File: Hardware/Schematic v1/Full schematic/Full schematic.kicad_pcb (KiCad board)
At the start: 2 copper layers, 159.3 x 59.9 mm, 329 parts, among them J1 Conn_01x02_Male, J10 Conn_01x01_Male, J2 Reset, J3 Encoder, J4 Failure LED, J5 Bluetooth, J6 Conn_01x02_Male, J7 Display, J8 Buttons, J9 Conn_01x02_Male, K1 EDR101A0500, K2 EDR101A0500, K3 EDR101A0500, K4 EDR101A0500, K5 EDR101A0500, K6 EDR101A0500, Q1 BC847, Q10 IRLML6402, Q11 BC847, Q12 IRFZ44, Q13 BC847, Q14 BSS138, Q15 BC847, Q16 IRF610, Q17 BC847, Q18 IRLML6402, Q19 BC847, Q2 BC847, Q20 BFS17, Q21 IRLML6402, Q22 AFT05MS003N, Q23 IRLML2502, Q24 IRLML2502, Q25 IRLML2502, Q26 IRLML2502, Q27 IRLML2502, Q28 IRLML2502, Q3 BC847, Q4 BC847, Q5 BC847, Q6 IRLML6402, Q7 IRF4905, Q8 IRLML6402, Q9 IRLML6402, U1 74LVC2T45DC, U10 ICS501, U11 STM32F103C8Tx, U12 CAT24C256, U2 74LVC2T45DC, U3 AD9835, U4 LM27313XMF, U5 LM2734X, U6 LM2734X, U7 LM2734X, U8 UC3843_SOIC8, U9 AD5245BRJZ10, X1 50MHz, Y1 8MHz, Y2 32768Hz

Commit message: Prepared to start PCB tracing
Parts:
- removed C107: 200pF, Capacitor_SMD:C_0805_2012Metric_Pad1.18x1.45mm_HandSolder
- removed C108, C109, C112: 0.1uF, Capacitor_SMD:C_0805_2012Metric_Pad1.18x1.45mm_HandSolder
- removed C110: 100uF x 16V, Capacitor_THT:CP_Radial_D6.3mm_P2.50mm
- removed C111: 22uF x 10V, Capacitor_THT:CP_Radial_D4.0mm_P2.00mm
- removed C113: 56pF, Capacitor_SMD:C_0805_2012Metric_Pad1.18x1.45mm_HandSolder
- removed C114, C115, C116, C117, C118, C119: 100pF, Capacitor_SMD:C_0805_2012Metric_Pad1.18x1.45mm_HandSolder
- removed C120, C121, C122, C123, C124, C125: 47pF, Capacitor_SMD:C_0805_2012Metric_Pad1.18x1.45mm_HandSolder
- removed C126, C127, C128, C129, C130, C131: 24pF, Capacitor_SMD:C_0805_2012Metric_Pad1.18x1.45mm_HandSolder
- removed C132, C133, C134, C135, C136, C137: 12pF, Capacitor_SMD:C_0805_2012Metric_Pad1.18x1.45mm_HandSolder
- removed D14: 1N4728A, Diode_THT:D_DO-41_SOD81_P10.16mm_Horizontal
- added Q29: IRLML2502, Package_TO_SOT_SMD:SOT-23, F.Cu at (104.5, 174.7)
- added Q30: IRLML2502, Package_TO_SOT_SMD:SOT-23, F.Cu at (172.8, 109.2)
- added R98: 100, Resistor_SMD:R_0805_2012Metric_Pad1.20x1.40mm_HandSolder, F.Cu at (138.6, 164.3)
- added R99: 100, Resistor_SMD:R_0805_2012Metric_Pad1.20x1.40mm_HandSolder, F.Cu at (119.0, 181.0)
- C1, C10, C11, C12, C18, C2, C3, C48, C7, C76, C8, C9, J1, J10, J2, J3, J4, J5, J6, J7, J8, J9, JP1, JP2, JP3, JP4, L13, L14, L15, L8, Q12, Q7, R45, R46, R88, R90, R92, RV1, RV2, X1, Y1, Y2: moved to F.Cu
- C100: value 0.1uF -> 56pF; moved to F.Cu
- C101: value 20pF -> 16pF 250V
- C102: value 200pF -> 8pF 250V
- C103: value 200pF -> 4pF 250V
- C104: value 200pF -> 2pF 250V
- C105: value 200pF -> 0.1uF
- C106: value 200pF -> 22uF x 10V; footprint Capacitor_SMD:C_0805_2012Metric_Pad1.18x1.45mm_HandSolder -> Capacitor_THT:CP_Radial_D4.0mm_P2.00mm
- C23, C85: value 4.7uF -> 0.1uF; moved to F.Cu
- C24, C65: value 0.1uF -> 4.7uF
- C28: value 10nF -> 1000uF x 10V; footprint Capacitor_SMD:C_0805_2012Metric_Pad1.18x1.45mm_HandSolder -> Capacitor_THT:CP_Radial_D10.0mm_P5.00mm
- C29: value 1000uF x 10V -> 47pF; footprint Capacitor_THT:CP_Radial_D10.0mm_P5.00mm -> Capacitor_SMD:C_0805_2012Metric_Pad1.18x1.45mm_HandSolder; moved to F.Cu
- C31: value 47pF -> 10nF
- C32: value 10nF -> 100pF
- C33: value 100pF -> 1nF
- C39, C55: value 1nF -> 4.7uF
- C41: value 1nF -> 47pF
- C44: value 47pF -> 220uFx6.3V; footprint Capacitor_SMD:C_0805_2012Metric_Pad1.18x1.45mm_HandSolder -> Capacitor_THT:CP_Radial_D6.3mm_P2.50mm
- C47: value 4.7uF -> 220uFx6.3V; footprint Capacitor_SMD:C_0805_2012Metric_Pad1.18x1.45mm_HandSolder -> Capacitor_THT:CP_Radial_D6.3mm_P2.50mm
- C49: value 220uFx6.3V -> 1nF; footprint Capacitor_THT:CP_Radial_D6.3mm_P2.50mm -> Capacitor_SMD:C_0805_2012Metric_Pad1.18x1.45mm_HandSolder; moved to F.Cu
- C50: value 220uFx6.3V -> 4.7uF; footprint Capacitor_THT:CP_Radial_D6.3mm_P2.50mm -> Capacitor_SMD:C_0805_2012Metric_Pad1.18x1.45mm_HandSolder; moved to F.Cu
- C51: value 1nF -> 1000uF x 25V; footprint Capacitor_SMD:C_0805_2012Metric_Pad1.18x1.45mm_HandSolder -> Capacitor_THT:CP_Radial_D10.0mm_P5.00mm
- C52, C60, C67: value 4.7uF -> 0.1uF
- C53: value 1000uF x 25V -> 1nF; footprint Capacitor_THT:CP_Radial_D10.0mm_P5.00mm -> Capacitor_SMD:C_0805_2012Metric_Pad1.18x1.45mm_HandSolder; moved to F.Cu
- C57: value 4.7uF -> 1000uF x 25V; footprint Capacitor_SMD:C_0805_2012Metric_Pad1.18x1.45mm_HandSolder -> Capacitor_THT:CP_Radial_D10.0mm_P5.00mm
- C58: value 1000uF x 25V -> 4.7uF; footprint Capacitor_THT:CP_Radial_D10.0mm_P5.00mm -> Capacitor_SMD:C_0805_2012Metric_Pad1.18x1.45mm_HandSolder; moved to F.Cu
- C61, C74: value 0.1uF -> 10nF
- C63, C93: value 10nF -> 0.1uF
- C68: value 0.1uF -> 1nF
- C70: value 0.1uF -> 75pF
- C71: value 1nF -> 10nF
- C72: value 75pF -> 0.1uF
- C73: value 10nF -> 100uFx6.3V; footprint Capacitor_SMD:C_0805_2012Metric_Pad1.18x1.45mm_HandSolder -> Capacitor_THT:CP_Radial_D6.3mm_P2.50mm
- C75: value 100uFx6.3V -> 1nF; footprint Capacitor_THT:CP_Radial_D6.3mm_P2.50mm -> Capacitor_SMD:C_0805_2012Metric_Pad1.18x1.45mm_HandSolder; moved to F.Cu
- C77: value 1nF -> 22pF
- C78: value 10nF -> 22pF; moved to F.Cu
- C79: value 22pF -> 10nF
- C80: value 22pF -> 8pF
- C81: value 10nF -> 8pF; moved to F.Cu
- C82: value 8pF -> 75pF
- C83: value 8pF -> 4.7uF
- C84: value 75pF -> 2pF 250V
- C86: value 0.1uF -> 62pF 250V; moved to F.Cu
- C87, C89: value 390pF -> 10nF
- C88, C92: value 390pF -> 0.1uF
- C90, C91: value 390pF -> 1nF
- C94: value 0.1uF -> 32pF 250V; moved to F.Cu
- C95: value 10nF -> 20pF
- C96, C97: value 1nF -> 0.1uF
- C98: value 0.1uF -> 100uF x 16V; footprint Capacitor_SMD:C_0805_2012Metric_Pad1.18x1.45mm_HandSolder -> Capacitor_THT:CP_Radial_D6.3mm_P2.50mm; moved to F.Cu
- D11: value 1N4148W -> 1N5819; footprint Diode_SMD:D_SOD-123 -> Diode_THT:D_DO-27_P5.08mm_Vertical_AnodeUp
- D12: value 1N5819 -> 1N4148W; footprint Diode_THT:D_DO-27_P5.08mm_Vertical_AnodeUp -> Diode_SMD:D_SOD-123; moved to F.Cu
- D13: value 1N4148W -> 1N4728A; footprint Diode_SMD:D_SOD-123 -> Diode_THT:D_DO-41_SOD81_P10.16mm_Horizontal
- K1, K2, K3, K4, K5, K6: value EDR101A0500 -> G6L-1F-DC5; footprint Relay_THT:Relay_SPST_StandexMeder_SIL_Form1A -> SamacSys:G6L-1F-DC5; moved to F.Cu
- L12: value 21uH -> 13uH; moved to F.Cu
- L5: value 10uH -> 22uH
- Q14: value BSS138 -> IRLML6402
- Q16: value IRF610 -> BSS138; footprint Package_TO_SOT_THT:TO-220-3_Vertical -> Package_TO_SOT_SMD:SOT-23; moved to F.Cu
- Q18: value IRLML6402 -> IRF610; footprint Package_TO_SOT_SMD:SOT-23 -> Package_TO_SOT_THT:TO-220-3_Vertical
- Q20: value BFS17 -> IRLML6402
- Q21: value IRLML6402 -> BC847
- Q22: value AFT05MS003N -> IRLML6402; footprint Package_TO_SOT_SMD:SOT-89-3_Handsoldering -> Package_TO_SOT_SMD:SOT-23
- Q23: value IRLML2502 -> BFS17
- Q24: value IRLML2502 -> AFT05MS003N; footprint Package_TO_SOT_SMD:SOT-23 -> Package_TO_SOT_SMD:SOT-89-3_Handsoldering
- R23: value 10k -> 47k
- R24, R70: value 4.7k -> 10k
- R25, R89, R93, R94: value 100 -> 4.7k
- R28: value 1.3k -> 100
- R29: value 150k -> 1.3k
- R30: value 12k -> 300
- R31: value 300 -> 150k
- R32: value 13k -> 12k
- R34: value 120k -> 13k
- R35: value 13k -> 120k
- R36: value 51k -> 13k
- R37: value 10k -> 51k
- R38: value 39k -> 10k
- R39, R77: value 10k -> 39k
- R40, R50: value 30k -> 10k
- R41: value 10k -> 10
- R42: value 10 -> 10k
- R43: value 10k -> 1k
- R44: value 1k -> 1; footprint Resistor_SMD:R_0805_2012Metric_Pad1.20x1.40mm_HandSolder -> Resistor_THT:R_Axial_DIN0207_L6.3mm_D2.5mm_P2.54mm_Vertical
- R47: value 1 -> 4.7k; footprint Resistor_THT:R_Axial_DIN0207_L6.3mm_D2.5mm_P2.54mm_Vertical -> Resistor_SMD:R_0805_2012Metric_Pad1.20x1.40mm_HandSolder; moved to F.Cu
- R48: value 4.7k -> 1; footprint Resistor_SMD:R_0805_2012Metric_Pad1.20x1.40mm_HandSolder -> Resistor_THT:R_Axial_DIN0207_L6.3mm_D2.5mm_P2.54mm_Vertical
- R49: value 1 -> 10k; footprint Resistor_THT:R_Axial_DIN0207_L6.3mm_D2.5mm_P2.54mm_Vertical -> Resistor_SMD:R_0805_2012Metric_Pad1.20x1.40mm_HandSolder; moved to F.Cu
- R51: value 6.8k -> 10
- R52: value 100 -> 30k
- R53: value 1k -> 6.8k
- R55: value 36k -> 1k
- R56: value 4.7k -> 100
- R57: value 56k -> 36k
- R58: value 30k -> 4.7k
- R59: value 6.8k -> 56k
- R60: value 1k -> 30k
- R61: value 100 -> 6.8k
- R62: value 3.9k -> 1k
- R63: value 2k -> 100
- R64: value 4.7k -> 3.9k
- R65: value 4.7k -> 2k
- R66: value 33k -> 4.7k
- R68: value 10k -> 33k
- R69: value 10k -> 4.7k
- R71: value 220k -> 4.7k
- R72: value 11k -> 10k
- R73: value 4.7k -> 220k
- R74: value 10 -> 11k
- R75: value 39k -> 4.7k
- R76: value 33 -> 10
- R78: value 4.7k -> 33
- R82: value 6.2k -> 10k
- R83: value 1k -> 4.7k
- R84: value 4.7k -> 6.2k
- R85: value 10 -> 1k
- R87: value 4.7k -> 10
- R91: value 4.7k -> 100; moved to F.Cu
- U7: value LM2734X -> MAX1837EUT33-T
- moved R34 153.7 mm to (191.8, 120.3), turned to 0 degrees
- moved R32 150.7 mm to (187.0, 120.4), turned to 0 degrees
- moved R30 149.4 mm to (191.3, 111.5), turned to 0 degrees
- moved R29 146.4 mm to (186.5, 114.5), turned to 0 degrees
- moved C30 141.0 mm to (176.9, 113.0), turned to 0 degrees
- moved C19 134.1 mm to (172.1, 113.0), turned to 0 degrees
- moved R37 133.7 mm to (182.3, 126.3), turned to 0 degrees
- moved C25 132.2 mm to (172.8, 125.0), turned to 0 degrees
- moved R39 130.9 mm to (191.3, 114.4), turned to 0 degrees
- moved L1 125.9 mm to (151.4, 109.5)
- moved C33 122.4 mm to (162.7, 120.8), turned to 0 degrees
- moved U5 120.7 mm to (162.3, 112.6), turned to 0 degrees
- moved L14 120.0 mm to (81.3, 128.3), turned to 0 degrees
- moved D5 119.1 mm to (162.6, 108.7), turned to 0 degrees
- moved Q3 118.4 mm to (167.3, 113.7), turned to 0 degrees
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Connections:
- C100 pad 1: REG_3.3V -> Net-(C100-Pad1)
- C101 pad 1: Net-(C101-Pad1) -> ANT_3.5
- C101 pad 2: GND -> Net-(C101-Pad2)
- C103 pad 1: Net-(C102-Pad2) -> ANT_3.5
- C104 pad 1: Net-(C103-Pad2) -> ANT_3.5
- C105 pad 1: Net-(C104-Pad2) -> PWR_3.5_5
- C105 pad 2: Net-(C105-Pad2) -> GND
- C106 pad 1: Net-(C105-Pad2) -> PWR_3.5_5
- C106 pad 2: Net-(C106-Pad2) -> GND
- C2 pad 1: REG_3.3V -> SW_3.3V
- C23 pad 1: PWR_3.5_12 -> Net-(C23-Pad1)
- C23 pad 2: GND -> Net-(C23-Pad2)
- C24 pad 1: Net-(C24-Pad1) -> PWR_3.5_12
- C24 pad 2: Net-(C24-Pad2) -> GND
- C28 pad 1: Net-(C28-Pad1) -> POWERS_3.5
- C28 pad 2: Net-(C28-Pad2) -> GND
- C29 pad 1: POWERS_3.5 -> Net-(C29-Pad1)
- C3 pad 1: REG_3.3V -> SW_3.3V
- C31 pad 2: GND -> Net-(C31-Pad2)
- C32 pad 1: Net-(C32-Pad1) -> Net-(C31-Pad1)
- C32 pad 2: Net-(C32-Pad2) -> GND
- C33 pad 1: Net-(C32-Pad1) -> REG_3.3V
- C39 pad 2: Net-(C39-Pad2) -> GND
- C41 pad 1: REG_5V -> Net-(C41-Pad1)
- C42 pad 1: DISPLAY_4V -> REG_5V
- C43 pad 1: REG_3.3V -> DISPLAY_4V
- C44 pad 1: Net-(C44-Pad1) -> REG_3.3V
- C47 pad 1: REG_3.3V -> REG_5V
- C48 pad 1: REG_5V -> DISPLAY_4V
- C49 pad 1: DISPLAY_4V -> Net-(C49-Pad1)
- C50 pad 1: REG_3.3V -> Net-(C49-Pad1)
- C51 pad 1: Net-(C51-Pad1) -> Net-(C49-Pad1)
- C52 pad 1: Net-(C51-Pad1) -> Net-(C52-Pad1)
- C52 pad 2: GND -> Net-(C52-Pad2)
- C53 pad 1: Net-(C51-Pad1) -> PWR_3.5_OUT
- C54 pad 2: Net-(C54-Pad2) -> Net-(C52-Pad1)
- C56 pad 1: Net-(C56-Pad1) -> PWR_3.5_12
- C56 pad 2: Net-(C54-Pad1) -> GND
- C58 pad 1: PWR_3.5_OUT -> PWR_3.5_12
- C59 pad 1: PWR_3.5_12 -> Net-(C59-Pad1)
- C59 pad 2: GND -> Net-(C59-Pad2)
- C60 pad 1: PWR_3.5_12 -> Net-(C60-Pad1)
- C61 pad 2: Net-(C61-Pad2) -> GND
- C62 pad 1: Net-(C62-Pad1) -> SW_3.3V
- C63 pad 2: GND -> Net-(C63-Pad2)
- C64 pad 1: REG_3.3V -> Net-(C64-Pad1)
- C65 pad 1: Net-(C65-Pad1) -> PWR_3.5_OUT
- C65 pad 2: Net-(C65-Pad2) -> GND
- C66 pad 1: Net-(C66-Pad1) -> PWR_3.5_OUT
- C67 pad 1: PWR_3.5_OUT -> Net-(C67-Pad1)
- C67 pad 2: GND -> Net-(C67-Pad2)
- C68 pad 1: PWR_3.5_OUT -> PWR_144_5
- C69 pad 1: Net-(C69-Pad1) -> RESET
- C69 pad 2: Net-(C69-Pad2) -> GND
- C70 pad 1: RESET -> Net-(C67-Pad1)
- C71 pad 1: PWR_144_5 -> Net-(C71-Pad1)
- C72 pad 1: Net-(C69-Pad1) -> PWR_144_5
- C73 pad 1: Net-(C73-Pad1) -> PWR_144_5
- C74 pad 1: PWR_144_5 -> ENCODER_BTN
- C75 pad 1: PWR_144_5 -> Net-(C75-Pad1)
- C75 pad 2: GND -> Net-(C75-Pad2)
- C76 pad 1: ENCODER_BTN -> ENCODER_R
- C77 pad 2: Net-(C77-Pad2) -> GND
- C78 pad 1: ENCODER_R -> Net-(C78-Pad1)
- C79 pad 1: Net-(C79-Pad1) -> ENCODER_L
- C81 pad 1: ENCODER_L -> Net-(C81-Pad1)
- C82 pad 2: GND -> Net-(C82-Pad2)
- C83 pad 1: Net-(C83-Pad1) -> REG_3.3V
- C84 pad 1: Net-(C84-Pad1) -> ANT_3.5
- C86 pad 1: REG_3.3V -> ANT_3.5
- C86 pad 2: GND -> Net-(C84-Pad2)
- C87 pad 1: ANT_3.5 -> BTN_RIGHT
- C87 pad 2: Net-(C87-Pad2) -> GND
- C88 pad 1: Net-(C87-Pad2) -> REG_3.3V
- C88 pad 2: Net-(C88-Pad2) -> GND
- C89 pad 1: Net-(C88-Pad2) -> BTN_LEFT
- C89 pad 2: Net-(C89-Pad2) -> GND
- C90 pad 1: Net-(C89-Pad2) -> PWR_144_OUT
- C90 pad 2: Net-(C90-Pad2) -> GND
- C91 pad 1: Net-(C90-Pad2) -> Net-(C91-Pad1)
- C92 pad 1: Net-(C91-Pad2) -> REG_3.3V
- C92 pad 2: Net-(C92-Pad2) -> GND
- C93 pad 1: BTN_RIGHT -> PWR_144_OUT
- C94 pad 1: REG_3.3V -> ANT_3.5
- C94 pad 2: GND -> Net-(C94-Pad2)
- C95 pad 1: BTN_LEFT -> Net-(C91-Pad1)
- C96 pad 1: PWR_144_OUT -> REG_3.3V
- C97 pad 1: Net-(C101-Pad1) -> GND
- C97 pad 2: Net-(C97-Pad2) -> SW_3.3V
- C98 pad 1: REG_3.3V -> PWR_144_OUT
- C99 pad 1: PWR_144_OUT -> REG_3.3V
- D10 pad 1: Net-(C28-Pad2) -> Net-(D10-Pad1)
- D10 pad 2: REG_3.3V -> Net-(D10-Pad2)
- D11 pad 1: Net-(D11-Pad1) -> Net-(C49-Pad1)
- D12 pad 1: Net-(C51-Pad1) -> Net-(C71-Pad1)
- D13 pad 1: Net-(C73-Pad1) -> ADC_UANT
- D13 pad 2: Net-(D13-Pad2) -> GND
- D7 pad 1: Net-(C28-Pad1) -> Net-(D7-Pad1)
- DA1 pad 3: Net-(C56-Pad1) -> Net-(C54-Pad1)
- J9 pad 2: Net-(C113-Pad1) -> Net-(C100-Pad1)
- K1 pad 1: Net-(C92-Pad2) -> Net-(C84-Pad2)
- K1 pad 3: PWR_3.5_5 -> Net-(K1-Pad3)
- K2 pad 1: Net-(C107-Pad2) -> Net-(C94-Pad2)
- K2 pad 3: PWR_3.5_5 -> Net-(K2-Pad3)
- K3 pad 1: Net-(C119-Pad2) -> Net-(C101-Pad2)
- K3 pad 3: PWR_3.5_5 -> Net-(K3-Pad3)
- K4 pad 1: Net-(C125-Pad2) -> Net-(C102-Pad2)
- K4 pad 3: PWR_3.5_5 -> Net-(K4-Pad3)
- K5 pad 1: Net-(C131-Pad2) -> Net-(C103-Pad2)
- K5 pad 3: PWR_3.5_5 -> Net-(K5-Pad3)
- K6 pad 1: Net-(C137-Pad2) -> Net-(C104-Pad2)
- K6 pad 3: PWR_3.5_5 -> Net-(K6-Pad3)
- L10 pad 1: Net-(C51-Pad1) -> Net-(C49-Pad1)
- L11 pad 2: Net-(C69-Pad2) -> Net-(C67-Pad2)
- L12 pad 1: Net-(C69-Pad1) -> Net-(C67-Pad1)
- L13 pad 2: Net-(C84-Pad2) -> Net-(C82-Pad2)
- L14 pad 2: Net-(C97-Pad2) -> Net-(C91-Pad2)
- L15 pad 1: Net-(C101-Pad1) -> Net-(C91-Pad1)
- L15 pad 2: Net-(C113-Pad1) -> Net-(C100-Pad1)
- L2 pad 1: Net-(C24-Pad1) -> Net-(C23-Pad1)
- L2 pad 2: Net-(C31-Pad1) -> Net-(C29-Pad1)
- L5 pad 1: Net-(C28-Pad1) -> Net-(D7-Pad1)
- L6 pad 1: Net-(C31-Pad1) -> Net-(C29-Pad1)
- L7 pad 2: Net-(C44-Pad1) -> Net-(C41-Pad1)
- L8 pad 2: Net-(D12-Pad2) -> Net-(D11-Pad2)
- L9 pad 1: Net-(C44-Pad1) -> Net-(C41-Pad1)
- L9 pad 2: Net-(C54-Pad1) -> Net-(C52-Pad1)
- Q12 pad 1: Net-(D11-Pad2) -> Net-(D10-Pad2)
- Q12 pad 2: Net-(D12-Pad2) -> Net-(D11-Pad2)
- Q13 pad 1: Net-(C54-Pad2) -> Net-(Q13-Pad1)
- Q13 pad 2: Net-(C62-Pad1) -> GND
- Q13 pad 3: Net-(C61-Pad2) -> Net-(Q13-Pad3)
- Q14 pad 2: GND -> REG_3.3V
- Q14 pad 3: Net-(C63-Pad1) -> SW_3.3V
- Q15 pad 1: Net-(C61-Pad1) -> Net-(C52-Pad2)
- Q15 pad 2: Net-(C66-Pad1) -> Net-(C60-Pad1)
- Q15 pad 3: Net-(C65-Pad2) -> Net-(C59-Pad2)
- Q16 pad 1: Net-(DA1-Pad6) -> Net-(Q16-Pad1)
- Q16 pad 2: Net-(C69-Pad2) -> GND
- Q16 pad 3: GND -> Net-(C61-Pad1)
- Q17 pad 1: Net-(Q17-Pad1) -> Net-(C59-Pad1)
- Q17 pad 2: GND -> Net-(C64-Pad1)
- Q17 pad 3: Net-(Q17-Pad3) -> Net-(C63-Pad2)
- Q18 pad 1: Net-(Q18-Pad1) -> Net-(DA1-Pad6)
- Q18 pad 2: REG_5V -> Net-(C67-Pad2)
- Q18 pad 3: BT_5V -> GND
- Q20 pad 1: Net-(C77-Pad1) -> Net-(Q20-Pad1)
- Q20 pad 2: GND -> REG_5V
- Q20 pad 3: Net-(C84-Pad2) -> BT_5V
- Q21 pad 2: PWR_144_5 -> GND
- Q21 pad 3: MANIP_144 -> Net-(Q21-Pad3)
- Q22 pad 1: Net-(C84-Pad1) -> Net-(Q22-Pad1)
- Q22 pad 2: GND -> PWR_144_5
- Q22 pad 3: Net-(C97-Pad2) -> MANIP_144
- Q23 pad 1: Net-(Q23-Pad1) -> Net-(C75-Pad1)
- Q23 pad 3: Net-(K1-Pad5) -> Net-(C82-Pad2)
- Q24 pad 1: Net-(Q24-Pad1) -> Net-(C82-Pad1)
- Q24 pad 3: Net-(K2-Pad5) -> Net-(C91-Pad2)
- Q25 pad 3: Net-(K3-Pad5) -> Net-(K1-Pad3)
- Q26 pad 3: Net-(K4-Pad5) -> Net-(K2-Pad3)
- Q27 pad 3: Net-(K5-Pad5) -> Net-(K3-Pad3)
- Q28 pad 3: Net-(K6-Pad5) -> Net-(K4-Pad3)
- R23 pad 1: Net-(Q6-Pad3) -> ACTIVATE_3.3V
- R23 pad 2: ADC_UBATT -> GND
- R24 pad 1: ADC_UBATT -> Net-(Q6-Pad3)
- R24 pad 2: GND -> ADC_UBATT
- R25 pad 1: Net-(R25-Pad1) -> ADC_UBATT
- R25 pad 2: Net-(R25-Pad2) -> GND
- R28 pad 1: Net-(Q11-Pad2) -> Net-(R28-Pad1)
- R28 pad 2: GND -> Net-(R28-Pad2)
- R29 pad 1: Net-(C19-Pad1) -> Net-(Q11-Pad2)
- R29 pad 2: Net-(C19-Pad2) -> GND
- R30 pad 1: Net-(C13-Pad1) -> Net-(C23-Pad2)
- R30 pad 2: Net-(C20-Pad1) -> GND
- R31 pad 1: Net-(C24-Pad2) -> Net-(C19-Pad1)
- R31 pad 2: GND -> Net-(C19-Pad2)
- R32 pad 1: Net-(C25-Pad2) -> Net-(C13-Pad1)
- R32 pad 2: GND -> Net-(C20-Pad1)
- R34 pad 1: PWR_3.5_12 -> Net-(C25-Pad2)
- R34 pad 2: Net-(C25-Pad2) -> GND
- R35 pad 1: Net-(C32-Pad2) -> PWR_3.5_12
- R35 pad 2: Net-(Q11-Pad2) -> Net-(C25-Pad2)
- R36 pad 1: REG_5V -> Net-(C31-Pad2)
- R36 pad 2: Net-(C37-Pad2) -> Net-(Q11-Pad2)
- R37 pad 1: Net-(C37-Pad2) -> REG_5V
- R37 pad 2: GND -> Net-(C37-Pad2)
- R38 pad 1: DISPLAY_4V -> Net-(C37-Pad2)
- R38 pad 2: Net-(C38-Pad2) -> GND
- R39 pad 1: Net-(C38-Pad2) -> DISPLAY_4V
- R39 pad 2: GND -> Net-(C38-Pad2)
- R40 pad 1: REG_3.3V -> Net-(C38-Pad2)
- R40 pad 2: Net-(C39-Pad2) -> GND
- R41 pad 1: Net-(C39-Pad2) -> Net-(D10-Pad2)
- R41 pad 2: GND -> Net-(D10-Pad1)
- R42 pad 1: Net-(D11-Pad2) -> Net-(D10-Pad2)
- R42 pad 2: Net-(D11-Pad1) -> GND
- R43 pad 1: Net-(D11-Pad2) -> Net-(Q12-Pad3)
- R43 pad 2: GND -> Net-(C31-Pad1)
- R44 pad 2: Net-(C32-Pad1) -> GND
- R47 pad 1: Net-(Q12-Pad3) -> Net-(C52-Pad1)
- R48 pad 1: Net-(C54-Pad1) -> Net-(Q12-Pad3)
- R49 pad 1: Net-(Q12-Pad3) -> Net-(Q13-Pad1)
- R49 pad 2: GND -> ACTIVATE_3.3V
- R50 pad 1: PWR_144_5 -> REG_3.3V
- R50 pad 2: Net-(C54-Pad2) -> Net-(Q14-Pad1)
- R51 pad 1: Net-(C54-Pad2) -> Net-(Q14-Pad1)
- R51 pad 2: GND -> Net-(Q13-Pad3)
- R52 pad 1: Net-(Q14-Pad1) -> PWR_144_5
- R52 pad 2: Manipulation -> Net-(C52-Pad2)
- R53 pad 1: PWR_144_5 -> Net-(C52-Pad2)
- R53 pad 2: Net-(C61-Pad2) -> GND
- R54 pad 1: Net-(C62-Pad1) -> Net-(Q16-Pad1)
- R54 pad 2: GND -> Manipulation
- R55 pad 1: PWR_3.5_OUT -> PWR_144_5
- R55 pad 2: Net-(C19-Pad2) -> Net-(C59-Pad2)
- R56 pad 1: Net-(C19-Pad2) -> Net-(C60-Pad1)
- R56 pad 2: Net-(R56-Pad2) -> GND
- R57 pad 1: PWR_3.5_12 -> PWR_3.5_OUT
- R57 pad 2: Net-(C63-Pad1) -> Net-(C19-Pad2)
- R58 pad 1: PWR_144_5 -> Net-(C19-Pad2)
- R58 pad 2: Net-(C61-Pad1) -> Net-(R58-Pad2)
- R59 pad 1: Net-(C61-Pad1) -> PWR_3.5_12
- R59 pad 2: GND -> Net-(C61-Pad1)
- R60 pad 2: Net-(C65-Pad2) -> Net-(C59-Pad1)
- R61 pad 1: Net-(C66-Pad1) -> Net-(C59-Pad1)
- R62 pad 1: Net-(DA1-Pad6) -> PWR_144_5
- R62 pad 2: Net-(DA1-Pad2) -> Net-(C63-Pad2)
- R63 pad 1: Net-(DA1-Pad2) -> Net-(C64-Pad1)
- R64 pad 1: PWR_144_5 -> Net-(DA1-Pad6)
- R64 pad 2: Net-(C65-Pad1) -> Net-(DA1-Pad2)
- R65 pad 1: Net-(C65-Pad1) -> Net-(DA1-Pad2)
- R66 pad 1: PWR_3.5_OUT -> PWR_144_5
- R66 pad 2: ADC_U3.5_OUT -> Net-(C63-Pad1)
- R67 pad 1: ADC_U3.5_OUT -> Net-(C63-Pad1)
- R68 pad 1: Net-(Q17-Pad1) -> PWR_3.5_OUT
- R68 pad 2: ENABLE_BT -> ADC_U3.5_OUT
- R69 pad 1: REG_5V -> ADC_U3.5_OUT
- R69 pad 2: Net-(Q18-Pad1) -> GND
- R70 pad 1: PWR_144_5 -> Net-(Q19-Pad1)
- R70 pad 2: Net-(R70-Pad2) -> ENABLE_BT
- R71 pad 1: ANT_3.5 -> PWR_144_5
- R71 pad 2: Net-(D13-Pad2) -> Net-(R71-Pad2)
- R72 pad 1: Net-(D13-Pad2) -> REG_5V
- R72 pad 2: GND -> Net-(Q20-Pad1)
- R73 pad 1: REG_3.3V -> ANT_3.5
- R73 pad 2: RESET -> Net-(D12-Pad2)
- R74 pad 1: Net-(Q18-Pad1) -> Net-(D12-Pad2)
- R74 pad 2: Net-(Q17-Pad3) -> GND
- R75 pad 1: ADC_UANT -> REG_3.3V
- R75 pad 2: Net-(C73-Pad1) -> RESET
- R76 pad 1: Net-(C77-Pad2) -> Net-(Q20-Pad1)
- R76 pad 2: GND -> Net-(Q19-Pad3)
- R77 pad 2: GND -> Net-(C71-Pad1)
- R78 pad 1: REG_3.3V -> Net-(C75-Pad2)
- R78 pad 2: ENCODER_BTN -> GND
- R79 pad 1: Net-(Q19-Pad1) -> ADC_UANT
- R79 pad 2: Manipulation -> GND
- R80 pad 1: REG_3.3V -> SW_3.3V
- R80 pad 2: ENCODER_R -> ENCODER_BTN
- R81 pad 1: PWR_144_5 -> Net-(Q21-Pad1)
- R81 pad 2: Net-(Q21-Pad1) -> Manipulation
- R82 pad 2: Net-(C77-Pad1) -> Net-(Q22-Pad1)
- R83 pad 1: Net-(C77-Pad1) -> SW_3.3V
- R83 pad 2: GND -> ENCODER_R
- R84 pad 1: REG_3.3V -> PWR_144_5
- R84 pad 2: ENCODER_L -> Net-(C75-Pad1)
- R85 pad 1: Net-(Q21-Pad1) -> Net-(C75-Pad1)
- R85 pad 2: Net-(Q19-Pad3) -> GND
- R86 pad 1: REG_3.3V -> SW_3.3V
- R86 pad 2: DISPLAY_SCL -> ENCODER_L
- R87 pad 1: REG_3.3V -> Net-(Q22-Pad1)
- R87 pad 2: DISPLAY_SDA -> Net-(Q21-Pad3)
- R88 pad 1: REG_3.3V -> SW_3.3V
- R88 pad 2: BTN_RIGHT -> DISPLAY_SCL
- R89 pad 1: Net-(Q23-Pad1) -> SW_3.3V
- R89 pad 2: MATCH_5 -> DISPLAY_SDA
- R90 pad 1: REG_3.3V -> SW_3.3V
- R90 pad 2: I2C2_SCL -> BTN_RIGHT
- R91 pad 1: REG_3.3V -> Net-(Q25-Pad1)
- R91 pad 2: BTN_LEFT -> MATCH_5
- R92 pad 1: REG_3.3V -> SW_3.3V
- R92 pad 2: I2C2_SDA -> I2C2_SCL
- R93 pad 1: Net-(Q24-Pad1) -> SW_3.3V
- R93 pad 2: MATCH_4 -> BTN_LEFT
- R94 pad 1: Net-(Q25-Pad1) -> SW_3.3V
- R94 pad 2: MATCH_3 -> I2C2_SDA
- R95 pad 2: MATCH_2 -> MATCH_4
- R96 pad 2: MATCH_1 -> MATCH_3
- R97 pad 2: MATCH_0 -> MATCH_2
- RV1 pad 2: Net-(C56-Pad1) -> Net-(C54-Pad1)
- RV1 pad 3: Net-(C63-Pad1) -> Net-(C61-Pad1)
- RV2 pad 2: Net-(C84-Pad1) -> Net-(C82-Pad1)
- U1 pad 1: REG_3.3V -> SW_3.3V
- U1 pad 5: REG_3.3V -> SW_3.3V
- U1 pad 6: Net-(R25-Pad2) -> Net-(R26-Pad2)
- U1 pad 7: Net-(R27-Pad2) -> Net-(R28-Pad2)
- U10 pad 1: Net-(C65-Pad1) -> Net-(C63-Pad1)
- U10 pad 5: Net-(C77-Pad2) -> Net-(C75-Pad2)
- U10 pad 7: Net-(R70-Pad2) -> Net-(R71-Pad2)
- U10 pad 8: Net-(U10-Pad8) -> unconnected-(U10-Pad8)
- U11 pad 28: Net-(U11-Pad28) -> ACTIVATE_3.3V
- U11 pad 3: Net-(C82-Pad1) -> Net-(C80-Pad1)
- U11 pad 4: Net-(C83-Pad1) -> Net-(C81-Pad1)
- U11 pad 5: Net-(C79-Pad1) -> Net-(C77-Pad1)
- U11 pad 6: Net-(C80-Pad1) -> Net-(C78-Pad1)
- U12 pad 8: REG_3.3V -> SW_3.3V
- U2 pad 1: REG_3.3V -> SW_3.3V
- U2 pad 5: REG_3.3V -> SW_3.3V
- U2 pad 6: Net-(U2-Pad6) -> unconnected-(U2-Pad6)
- U2 pad 7: Net-(R26-Pad2) -> Net-(R27-Pad2)
- U3 pad 14: Net-(C24-Pad2) -> Net-(C23-Pad2)
- U3 pad 7: Net-(R27-Pad1) -> Net-(R28-Pad1)
- U3 pad 8: Net-(R25-Pad1) -> Net-(R26-Pad1)
- U3 pad 9: Net-(R26-Pad1) -> Net-(R27-Pad1)
- U7 pad 1: Net-(C28-Pad2) -> GND
- U7 pad 3: Net-(C39-Pad2) -> BATT_7.4V
- U7 pad 4: BATT_7.4V -> Net-(D7-Pad1)
- U7 pad 6: Net-(C28-Pad1) -> REG_3.3V
- U8 pad 3: Net-(C32-Pad1) -> Net-(C31-Pad1)
- U8 pad 6: Net-(D11-Pad1) -> Net-(D10-Pad1)
- U9 pad 1: Net-(R56-Pad2) -> Net-(R58-Pad2)
- U9 pad 2: REG_3.3V -> SW_3.3V
- U9 pad 8: Net-(R56-Pad2) -> Net-(R58-Pad2)
- X1 pad 1: Net-(X1-Pad1) -> unconnected-(X1-Pad1)
- Y1 pad 1: Net-(C80-Pad1) -> Net-(C78-Pad1)
- Y1 pad 2: Net-(C79-Pad1) -> Net-(C77-Pad1)
- Y2 pad 1: Net-(C83-Pad1) -> Net-(C81-Pad1)
- Y2 pad 2: Net-(C82-Pad1) -> Net-(C80-Pad1)
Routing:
- net GND: track 906.1 -> 0.00 mm, vias 80 -> 0
- net ACTIVATE_144: track 324.4 -> 0.00 mm, vias 2 -> 0
- net REG_5V: track 232.8 -> 0.00 mm, vias 11 -> 0
- net REG_3.3V: track 228.3 -> 0.00 mm, vias 16 -> 0
- net PWR_3.5_5: track 224.5 -> 0.00 mm, vias 3 -> 0
- net MATCH_2: track 218.8 -> 0.00 mm, vias 7 -> 0
- net BATT_7.4V: track 197.2 -> 0.00 mm, vias 1 -> 0
- net MATCH_1: track 196.9 -> 0.00 mm, vias 6 -> 0
- net PWR_3.5_12: track 188.5 -> 0.00 mm, vias 8 -> 0
- net ACTIVATE_DISPLAY: track 184.9 -> 0.00 mm, vias 3 -> 0
- net ACTIVATE_FOX: track 164.8 -> 0.00 mm, vias 2 -> 0
- net ADC_UANT: track 142.9 -> 0.00 mm, vias 2 -> 0
- net Manipulation: track 137.6 -> 0.00 mm, vias 6 -> 0
- net MATCH_0: track 119.7 -> 0.00 mm, vias 2 -> 0
- net MATCH_5: track 119.0 -> 0.00 mm, vias 6 -> 0
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- removed copper zone on B.Cu, net GND
- removed copper zone on F.Cu, net GND
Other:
- board outline removed
- net class Default removed
- board text removed: "https://github.com/WhiteFossa/yiff-l"

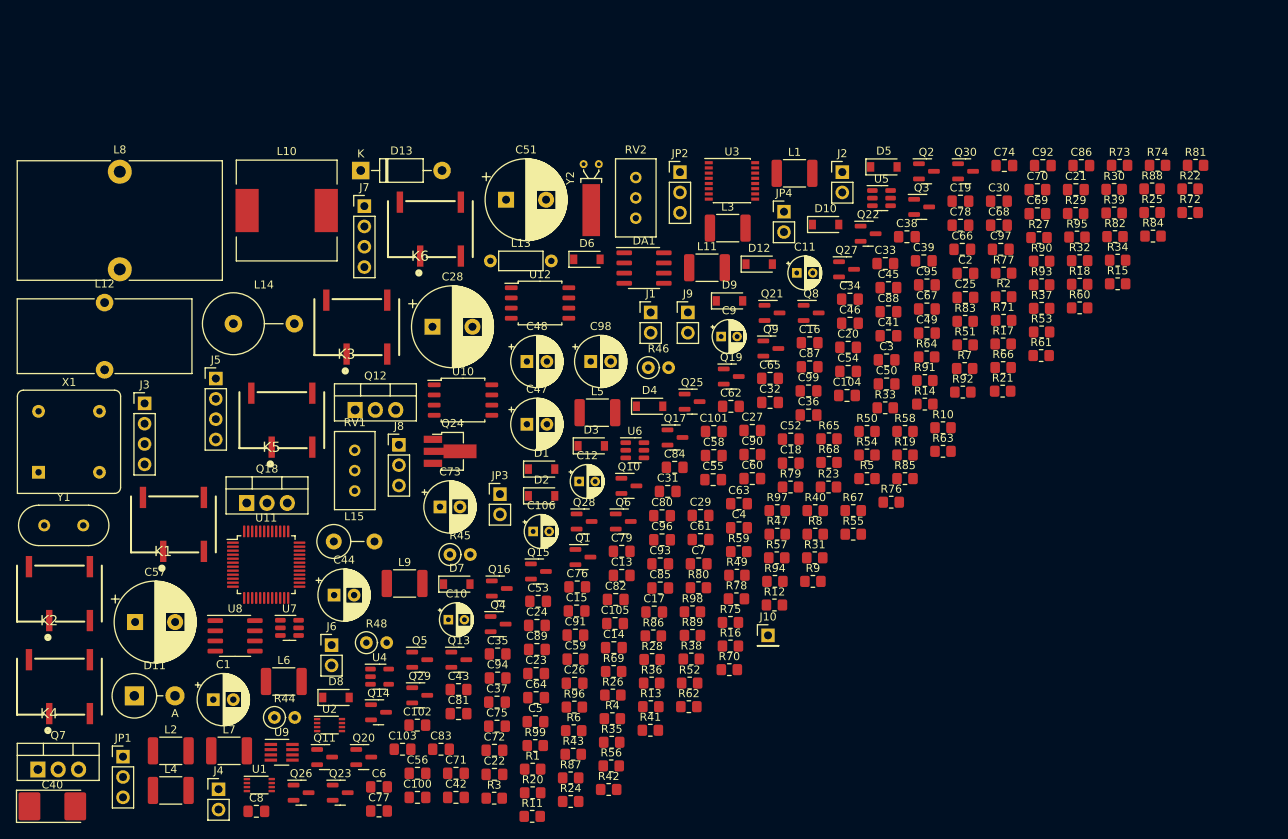
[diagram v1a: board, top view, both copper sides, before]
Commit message: All inductors are SMD now
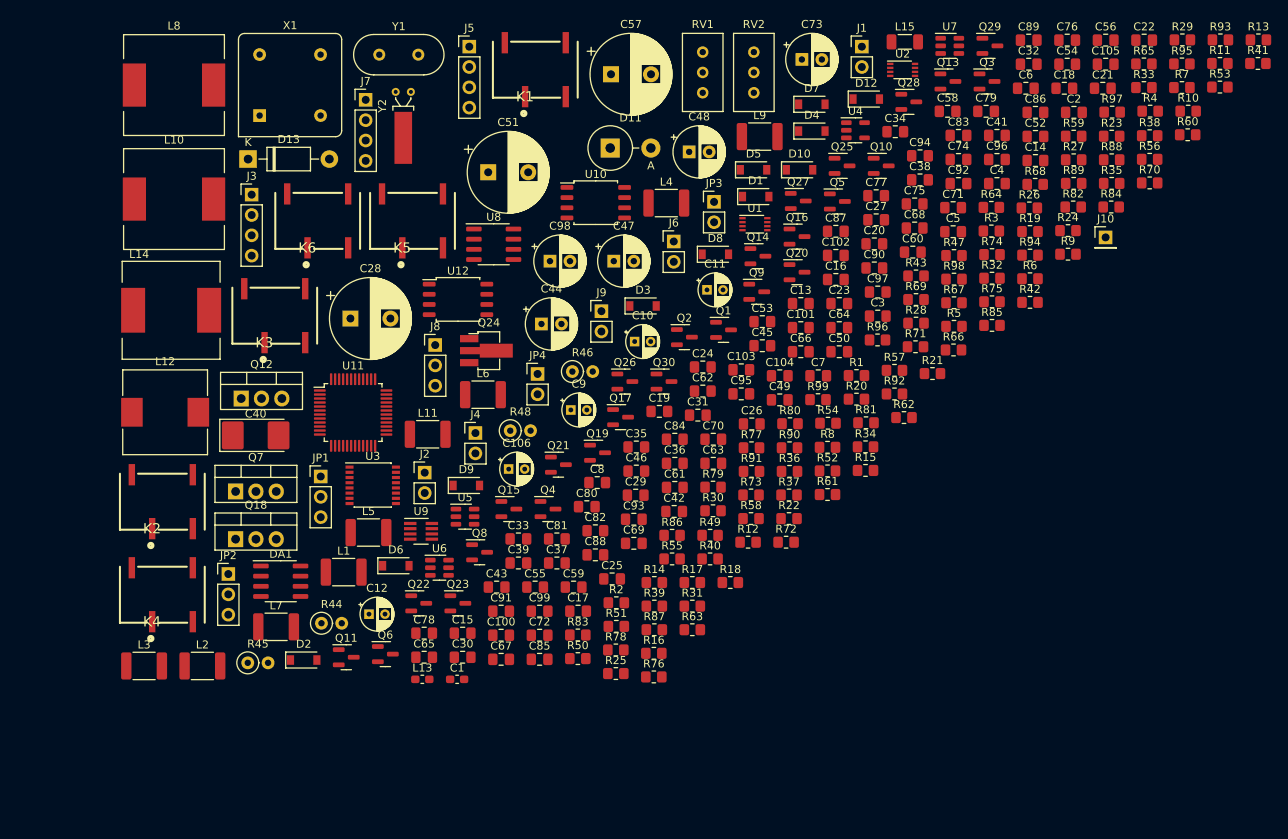
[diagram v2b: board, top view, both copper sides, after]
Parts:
- C1: footprint Capacitor_THT:CP_Radial_D6.3mm_P2.50mm -> Inductor_SMD:L_0603_1608Metric_Pad1.05x0.95mm_HandSolder
- L12: footprint Inductor_THT:L_Toroid_Vertical_L21.6mm_W9.1mm_P8.40mm_Bourns_5700 -> Inductor_SMD:L_10.4x10.4_H4.8
- L13: footprint Inductor_THT:L_Axial_L5.3mm_D2.2mm_P7.62mm_Horizontal_Vishay_IM-1 -> Inductor_SMD:L_0603_1608Metric_Pad1.05x0.95mm_HandSolder
- L14: footprint Inductor_THT:L_Axial_L16.0mm_D7.5mm_P7.62mm_Vertical_Fastron_XHBCC -> Inductor_SMD:L_Pulse_PA4320
- L15: value 23.5nH -> 22nH; footprint Inductor_THT:L_Axial_L9.5mm_D4.0mm_P5.08mm_Vertical_Fastron_SMCC -> Inductor_SMD:L_1206_3216Metric_Pad1.22x1.90mm_HandSolder
- L8: footprint Inductor_THT:L_Toroid_Vertical_L25.4mm_W14.7mm_P12.20mm_Vishay_TJ5_BigPads -> Inductor_SMD:L_12x12mm_H8mm
- moved R11 127.5 mm to (204.6, 95.7)
- moved C56 125.7 mm to (190.3, 92.8)
- moved C22 122.6 mm to (195.1, 92.8)
- moved C6 119.0 mm to (180.3, 98.8)
- moved R41 112.8 mm to (209.3, 95.7)
- moved R13 112.8 mm to (209.4, 92.8)
- moved U7 110.0 mm to (170.8, 93.5)
- moved U2 108.8 mm to (164.9, 96.5)
- moved Q29 108.0 mm to (175.8, 93.5)
- moved R4 101.4 mm to (195.8, 101.7)
- moved R56 101.4 mm to (195.8, 107.7)
- moved C83 100.4 mm to (171.9, 104.7)
- moved C77 98.9 mm to (161.6, 112.3)
- moved C89 97.9 mm to (180.7, 92.8)
- moved L4 96.1 mm to (135.4, 113.2)
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
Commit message: - New antenna matcher
- Ready to trace PCB
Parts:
- removed JP3: SWDIO, Connector_PinHeader_2.54mm:PinHeader_1x02_P2.54mm_Vertical
- removed JP4: SWCLK, Connector_PinHeader_2.54mm:PinHeader_1x02_P2.54mm_Vertical
- removed Q25, Q26, Q27, Q28, Q29, Q30: IRLML2502, Package_TO_SOT_SMD:SOT-23
- removed R95, R96, R97, R98, R99: 100, Resistor_SMD:R_0805_2012Metric_Pad1.20x1.40mm_HandSolder
- added C107: 2pF 250V, Capacitor_SMD:C_0805_2012Metric_Pad1.18x1.45mm_HandSolder, F.Cu at (107.1, 172.7)
- added U13: CAT24C256, Package_SO:SOIC-8_5.23x5.23mm_P1.27mm, F.Cu at (80.0, 169.5)
- C100: value 56pF -> 22uF x 10V; footprint Capacitor_SMD:C_0805_2012Metric_Pad1.18x1.45mm_HandSolder -> Capacitor_THT:CP_Radial_D4.0mm_P2.00mm
- C101: value 16pF 250V -> 2pF 250V
- C102: value 8pF 250V -> 16pF 250V
- C104: value 2pF 250V -> 32pF 250V
- C105: value 0.1uF -> 8pF 250V
- C106: value 22uF x 10V -> 62pF 250V; footprint Capacitor_THT:CP_Radial_D4.0mm_P2.00mm -> Capacitor_SMD:C_0805_2012Metric_Pad1.18x1.45mm_HandSolder
- C84: value 2pF 250V -> 0.1uF
- C86: value 62pF 250V -> 10nF
- C87: value 10nF -> 0.1uF
- C88: value 0.1uF -> 10nF
- C89: value 10nF -> 1nF
- C91: value 1nF -> 0.1uF
- C93: value 0.1uF -> 20pF
- C94: value 32pF 250V -> 0.1uF
- C95: value 20pF -> 0.1uF
- C96: value 0.1uF -> 100uF x 16V; footprint Capacitor_SMD:C_0805_2012Metric_Pad1.18x1.45mm_HandSolder -> Capacitor_THT:CP_Radial_D6.3mm_P2.50mm
- C98: value 100uF x 16V -> 0.1uF; footprint Capacitor_THT:CP_Radial_D6.3mm_P2.50mm -> Capacitor_SMD:C_0805_2012Metric_Pad1.18x1.45mm_HandSolder
- C99: value 0.1uF -> 56pF
- J10: value Conn_01x01_Male -> Conn_01x03_Male; footprint Connector_PinHeader_2.54mm:PinHeader_1x01_P2.54mm_Vertical -> Connector_PinHeader_2.54mm:PinHeader_1x03_P2.54mm_Vertical
- K1, K2, K3, K4, K5, K6: value G6L-1F-DC5 -> IM43TS; footprint SamacSys:G6L-1F-DC5 -> Mouser:IM43TS
- L14: footprint Inductor_SMD:L_Pulse_PA4320 -> Mouser:2222SQ301GEC
- R91: value 100 -> 4.7k
- U12: value CAT24C256 -> MCP23017_SS; footprint Package_SO:SOIC-8_5.23x5.23mm_P1.27mm -> Package_SO:SSOP-28_5.3x10.2mm_P0.65mm
- moved C65 114.7 mm to (191.4, 94.4)
- moved R25 114.1 mm to (215.3, 97.3)
- moved R76 104.8 mm to (212.6, 103.2)
- moved C59 102.2 mm to (201.1, 94.4)
- moved Q6 98.8 mm to (174.2, 104.0)
- moved C67 98.7 mm to (188.7, 104.9)
- moved J1 98.5 mm to (96.8, 169.4)
- moved U2 98.5 mm to (101.9, 172.2)
- moved D6 98.2 mm to (176.1, 94.6)
- moved C89 97.9 mm to (121.9, 171.1)
- moved C32 97.3 mm to (117.1, 169.5)
- moved Q8 96.8 mm to (186.6, 95.1)
- moved C81 96.2 mm to (196.3, 94.4)
- moved R17 91.8 mm to (207.9, 100.3)
- moved C78 90.9 mm to (174.1, 107.8)
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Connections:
- C100 pad 1: Net-(C100-Pad1) -> PWR_3.5_5
- C101 pad 1: ANT_3.5 -> Net-(C101-Pad1)
- C101 pad 2: Net-(C101-Pad2) -> ANT_3.5
- C102 pad 1: ANT_3.5 -> Net-(C102-Pad1)
- C102 pad 2: Net-(C102-Pad2) -> ANT_3.5
- C103 pad 1: ANT_3.5 -> Net-(C103-Pad1)
- C103 pad 2: Net-(C103-Pad2) -> ANT_3.5
- C104 pad 1: ANT_3.5 -> Net-(C104-Pad1)
- C104 pad 2: Net-(C104-Pad2) -> ANT_3.5
- C105 pad 1: PWR_3.5_5 -> Net-(C105-Pad1)
- C105 pad 2: GND -> ANT_3.5
- C106 pad 1: PWR_3.5_5 -> Net-(C106-Pad1)
- C106 pad 2: GND -> ANT_3.5
- C84 pad 1: ANT_3.5 -> REG_3.3V
- C84 pad 2: Net-(C84-Pad2) -> GND
- C85 pad 1: REG_3.3V -> Net-(C85-Pad1)
- C86 pad 1: ANT_3.5 -> BTN_RIGHT
- C86 pad 2: Net-(C84-Pad2) -> GND
- C87 pad 1: BTN_RIGHT -> REG_3.3V
- C88 pad 1: REG_3.3V -> BTN_LEFT
- C89 pad 1: BTN_LEFT -> PWR_144_OUT
- C90 pad 1: PWR_144_OUT -> Net-(C90-Pad1)
- C90 pad 2: GND -> Net-(C90-Pad2)
- C91 pad 1: Net-(C91-Pad1) -> REG_3.3V
- C91 pad 2: Net-(C91-Pad2) -> GND
- C92 pad 1: REG_3.3V -> PWR_144_OUT
- C93 pad 1: PWR_144_OUT -> Net-(C90-Pad1)
- C94 pad 1: ANT_3.5 -> REG_3.3V
- C94 pad 2: Net-(C94-Pad2) -> GND
- C95 pad 1: Net-(C91-Pad1) -> GND
- C95 pad 2: GND -> SW_3.3V
- C96 pad 1: REG_3.3V -> PWR_144_OUT
- C97 pad 1: GND -> REG_3.3V
- C97 pad 2: SW_3.3V -> GND
- C98 pad 1: PWR_144_OUT -> PWR_3.5_5
- C99 pad 1: REG_3.3V -> Net-(C99-Pad1)
- J9 pad 2: Net-(C100-Pad1) -> Net-(C99-Pad1)
- K1 pad 1: Net-(C84-Pad2) -> MATCH0+
- K1 pad 2: GND -> unconnected-(K1-Pad2)
- K1 pad 3: Net-(K1-Pad3) -> GND
- K1 pad 4: PWR_3.5_5 -> Net-(C101-Pad1)
- K2 pad 1: Net-(C94-Pad2) -> MATCH3+
- K2 pad 2: GND -> unconnected-(K2-Pad2)
- K2 pad 3: Net-(K2-Pad3) -> GND
- K2 pad 4: PWR_3.5_5 -> Net-(C102-Pad1)
- K3 pad 1: Net-(C101-Pad2) -> MATCH1+
- K3 pad 2: GND -> unconnected-(K3-Pad2)
- K3 pad 3: Net-(K3-Pad3) -> GND
- K3 pad 4: PWR_3.5_5 -> Net-(C103-Pad1)
- K4 pad 1: Net-(C102-Pad2) -> MATCH4+
- K4 pad 2: GND -> unconnected-(K4-Pad2)
- K4 pad 3: Net-(K4-Pad3) -> GND
- K4 pad 4: PWR_3.5_5 -> Net-(C104-Pad1)
- K5 pad 1: Net-(C103-Pad2) -> MATCH2+
- K5 pad 2: GND -> unconnected-(K5-Pad2)
- K5 pad 3: Net-(K5-Pad3) -> GND
- K5 pad 4: PWR_3.5_5 -> Net-(C105-Pad1)
- K6 pad 1: Net-(C104-Pad2) -> MATCH5+
- K6 pad 2: GND -> unconnected-(K6-Pad2)
- K6 pad 3: Net-(K6-Pad3) -> GND
- K6 pad 4: PWR_3.5_5 -> Net-(C106-Pad1)
- L14 pad 2: Net-(C91-Pad2) -> Net-(C90-Pad2)
- L15 pad 1: Net-(C91-Pad1) -> Net-(C90-Pad1)
- L15 pad 2: Net-(C100-Pad1) -> Net-(C99-Pad1)
- Q24 pad 3: Net-(C91-Pad2) -> Net-(C90-Pad2)
- R90 pad 1: SW_3.3V -> PWR_3.5_5
- R90 pad 2: BTN_RIGHT -> Net-(C85-Pad1)
- R91 pad 1: Net-(Q25-Pad1) -> SW_3.3V
- R91 pad 2: MATCH_5 -> BTN_RIGHT
- U11 pad 13: MATCH_0 -> unconnected-(U11-Pad13)
- U11 pad 32: MATCH_1 -> unconnected-(U11-Pad32)
- U11 pad 33: MATCH_2 -> unconnected-(U11-Pad33)
- U11 pad 38: MATCH_5 -> unconnected-(U11-Pad38)
- U12 pad 1: GND -> MATCH0-
- U12 pad 2: GND -> MATCH1-
- U12 pad 3: GND -> MATCH2-
- U12 pad 4: GND -> MATCH3-
- U12 pad 5: I2C2_SDA -> MATCH4-
- U12 pad 6: I2C2_SCL -> MATCH5-
- U12 pad 7: GND -> unconnected-(U12-Pad7)
- U12 pad 8: SW_3.3V -> unconnected-(U12-Pad8)

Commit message: Partially traced new PCB
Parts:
- C100, C54, C56, C58, C70, C98, J6, K1, K2, K3, K4, K5, K6, Q18, R54, R64, R65, RV1: moved to B.Cu
- moved K6 281.3 mm to (348.5, 63.0), turned to 90 degrees
- moved C107 268.1 mm to (347.5, 54.1)
- moved C106 266.3 mm to (351.0, 54.1)
- moved K4 256.2 mm to (339.4, 63.0), turned to 90 degrees
- moved L12 248.4 mm to (345.6, 47.6)
- moved C104 243.8 mm to (340.5, 54.1)
- moved Q18 242.9 mm to (334.8, 47.1), turned to -90 degrees
- moved L11 240.0 mm to (337.8, 46.0), turned to -90 degrees
- moved C66 234.5 mm to (334.4, 43.6), turned to 180 degrees
- moved R64 228.3 mm to (332.9, 48.0), turned to -90 degrees
- moved DA1 228.0 mm to (328.2, 50.5)
- moved K3 226.9 mm to (312.3, 63.0), turned to 90 degrees
- moved RV1 226.8 mm to (330.2, 46.9), turned to 90 degrees
- moved K5 221.3 mm to (321.4, 63.0), turned to 90 degrees
- moved C54 218.3 mm to (324.8, 51.2), turned to 180 degrees
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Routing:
- net GND: track 0.00 -> 121.8 mm, vias 0 -> 5
- net ANT_3.5: track 0.00 -> 58.7 mm, vias 0 -> 7
- net MATCH0+: track 0.00 -> 47.2 mm, vias 0 -> 1
- net MATCH5-: track 0.00 -> 46.4 mm
- net MATCH1+: track 0.00 -> 33.5 mm, vias 0 -> 1
- net MATCH4-: track 0.00 -> 33.2 mm
- net MATCH0-: track 0.00 -> 20.2 mm
- net MATCH2+: track 0.00 -> 19.4 mm, vias 0 -> 1
- net MATCH5+: track 0.00 -> 18.8 mm
- net MATCH3-: track 0.00 -> 18.6 mm
- net MATCH4+: track 0.00 -> 13.8 mm
- net PWR_3.5_12: track 0.00 -> 12.8 mm, vias 0 -> 2
- net Net-(C67-Pad1): track 0.00 -> 10.3 mm, vias 0 -> 1
- net Net-(C61-Pad1): track 0.00 -> 9.29 mm
- net MATCH1-: track 0.00 -> 9.15 mm
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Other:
- board outline added: 120 x 48.3 mm

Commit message: - some schematic fixes
- PCB tracing in progress
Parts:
- added C101: 4.7uF, Capacitor_SMD:C_0805_2012Metric_Pad1.18x1.45mm_HandSolder, F.Cu at (302.3, 65.2)
- added C102: 4.7uF, Capacitor_SMD:C_0805_2012Metric_Pad1.18x1.45mm_HandSolder, F.Cu at (329.6, 65.2)
- added C103: 4.7uF, Capacitor_SMD:C_0805_2012Metric_Pad1.18x1.45mm_HandSolder, F.Cu at (303.9, 65.2)
- added C104: 4.7uF, Capacitor_SMD:C_0805_2012Metric_Pad1.18x1.45mm_HandSolder, F.Cu at (331.2, 65.2)
- added C107: 4.7uF, Capacitor_SMD:C_0805_2012Metric_Pad1.18x1.45mm_HandSolder, F.Cu at (311.5, 65.2)
- added C108: 4.7uF, Capacitor_SMD:C_0805_2012Metric_Pad1.18x1.45mm_HandSolder, F.Cu at (338.7, 65.2)
- added C109: 4.7uF, Capacitor_SMD:C_0805_2012Metric_Pad1.18x1.45mm_HandSolder, F.Cu at (313.2, 65.2)
- added C110: 4.7uF, Capacitor_SMD:C_0805_2012Metric_Pad1.18x1.45mm_HandSolder, F.Cu at (340.4, 65.2)
- added C113: 4.7uF, Capacitor_SMD:C_0805_2012Metric_Pad1.18x1.45mm_HandSolder, F.Cu at (320.7, 65.2)
- added C114: 4.7uF, Capacitor_SMD:C_0805_2012Metric_Pad1.18x1.45mm_HandSolder, F.Cu at (347.7, 65.2)
- added C115: 4.7uF, Capacitor_SMD:C_0805_2012Metric_Pad1.18x1.45mm_HandSolder, F.Cu at (322.3, 65.2)
- added C116: 4.7uF, Capacitor_SMD:C_0805_2012Metric_Pad1.18x1.45mm_HandSolder, F.Cu at (349.4, 65.2)
- added R88: 36k, Resistor_SMD:R_0805_2012Metric_Pad1.20x1.40mm_HandSolder, F.Cu at (103.1, 120.0)
- moved U12 3.12 mm to (327.6, 73.6)
- moved C100 3.12 mm to (321.8, 73.4)
- moved C98 3.12 mm to (325.8, 74.9)
- renumbered C101 to C105, C102 to C106, C103 to C111, C104 to C112, C105 to C117, C106 to C118, C107 to C119, R88 to R89, R89 to R90, R90 to R91, R91 to R92, R92 to R93, R93 to R94, R94 to R95
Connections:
- K1 pad 1: MATCH0+ -> Net-(C101-Pad1)
- K2 pad 1: MATCH3+ -> Net-(C102-Pad1)
- K3 pad 1: MATCH1+ -> Net-(C107-Pad1)
- K4 pad 1: MATCH4+ -> Net-(C108-Pad1)
- K5 pad 1: MATCH2+ -> Net-(C113-Pad1)
- K6 pad 1: MATCH5+ -> Net-(C114-Pad1)
- RV2 pad 1: MANIP_144 -> Net-(R88-Pad2)
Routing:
- net MATCH0+: track 47.2 -> 34.5 mm, vias 1 -> 0
- net MATCH1+: track 33.5 -> 25.0 mm, vias 1 -> 0
- net MATCH5-: track 46.4 -> 38.5 mm, vias 0 -> 1
- net MATCH5+: track 18.8 -> 23.8 mm
- net MATCH4-: track 33.2 -> 28.7 mm, vias 0 -> 1
- net MATCH1-: track 9.15 -> 12.9 mm, vias 0 -> 1
- net MATCH2+: track 19.4 -> 15.8 mm, vias 1 -> 0
- net MATCH2-: track 6.09 -> 9.67 mm, vias 0 -> 1
- net Net-(C107-Pad1): track 0.00 -> 2.99 mm
- net Net-(C114-Pad1): track 0.00 -> 2.97 mm
- net Net-(C113-Pad1): track 0.00 -> 2.97 mm
- net Net-(C101-Pad1): track 0.00 -> 2.97 mm
- net Net-(C102-Pad1): track 0.00 -> 2.95 mm
- net Net-(C108-Pad1): track 0.00 -> 2.95 mm
- net MATCH4+: track 13.8 -> 16.2 mm
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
